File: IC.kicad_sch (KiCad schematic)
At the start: 24 parts, among them IC1 BTS722204ESAXUMA1

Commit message: Minor fixes
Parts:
- removed IC1: BTS722204ESAXUMA1, Samacsys:SOP65P600X115-25N, symbol Samacsys_kicad_sym:BTS722204ESAXUMA1
- added IC5: BTS722204ESAXUMA1, SOP65P600X115-25N, symbol BTS722204ESAXUMA1:BTS722204ESAXUMA1
- R16, R17, R18: value 1.2k -> 330
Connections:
- net IN0: now also IC5.8 (IN0)
- net IN1: now also IC5.9 (IN1)
- net IN2: now also IC5.10 (IN2)
- net IN3: now also IC5.11 (IN3)
- net OUT0: now also IC5.21 (OUT0_1), IC5.22 (OUT0_2), IC5.23 (OUT0_3), IC5.24 (OUT0_4)
- net OUT1: now also IC5.19 (OUT1_1), IC5.20 (OUT1_2)
- net OUT2: now also IC5.17 (OUT2_1), IC5.18 (OUT2_2)
- net OUT3: now also IC5.13 (OUT3_1), IC5.14 (OUT3_2), IC5.15 (OUT3_3), IC5.16 (OUT3_4)
- net VS: now also IC5.25 (VS)
- net at R18.2: now also IC5.6 (CSN)
- net at C19.2, C20.1, R14.2: now also IC5.1 (GND_1)
- net at R13.1, R8.2: now also IC5.12 (IS)
- net at C20.2, R7.2: now also IC5.2 (VDD)
- net at R15.2: now also IC5.3 (SO)
- net at R16.2: now also IC5.4 (SI)
- net at R17.2: now also IC5.5 (SCLK)
- net at R6.2: now also IC5.7 (LHI)

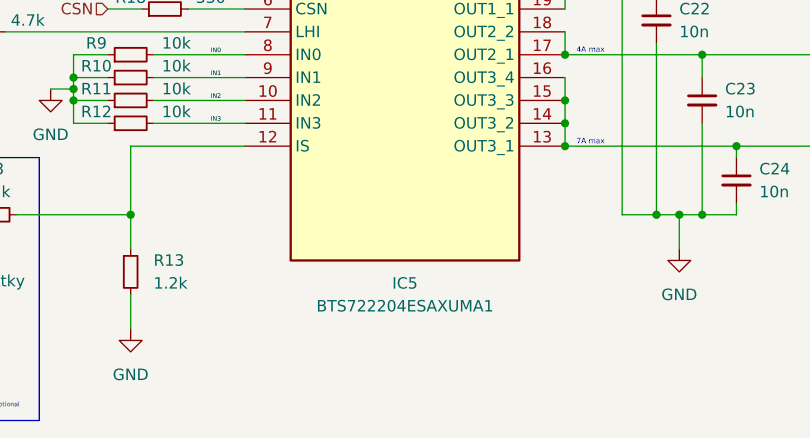
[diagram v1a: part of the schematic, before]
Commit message: Footprint changes + started PCB
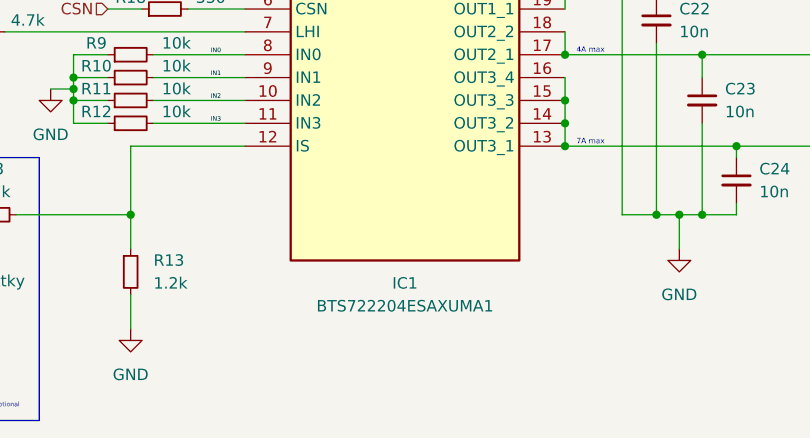
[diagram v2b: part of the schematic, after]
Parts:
- removed IC5: BTS722204ESAXUMA1, SOP65P600X115-25N, symbol BTS722204ESAXUMA1:BTS722204ESAXUMA1
- added IC1: BTS722204ESAXUMA1, SOP65P600X115-25N, symbol BTS722204ESAXUMA1:BTS722204ESAXUMA1
- R15, R16, R17, R18, R6: footprint Resistor_SMD:R_0603_1608Metric -> Resistor_SMD:R_0603_1608Metric_Pad0.98x0.95mm_HandSolder
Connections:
- net IN0: now also IC1.8 (IN0)
- net IN1: now also IC1.9 (IN1)
- net IN2: now also IC1.10 (IN2)
- net IN3: now also IC1.11 (IN3)
- net OUT0: now also IC1.21 (OUT0_1), IC1.22 (OUT0_2), IC1.23 (OUT0_3), IC1.24 (OUT0_4)
- net OUT1: now also IC1.19 (OUT1_1), IC1.20 (OUT1_2)
- net OUT2: now also IC1.17 (OUT2_1), IC1.18 (OUT2_2)
- net OUT3: now also IC1.13 (OUT3_1), IC1.14 (OUT3_2), IC1.15 (OUT3_3), IC1.16 (OUT3_4)
- net VS: now also IC1.25 (VS)
- net at R18.2: now also IC1.6 (CSN)
- net at R13.1, R8.2: now also IC1.12 (IS)
- net at C19.2, C20.1, R14.2: now also IC1.1 (GND_1)
- net at C20.2, R7.2: now also IC1.2 (VDD)
- net at R15.2: now also IC1.3 (SO)
- net at R16.2: now also IC1.4 (SI)
- net at R17.2: now also IC1.5 (SCLK)
- net at R6.2: now also IC1.7 (LHI)
